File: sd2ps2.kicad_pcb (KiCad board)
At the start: 2 copper layers, 36 x 52.5 mm, 11 parts, among them J1 Conn_01x08, J2 DM3AT-SF-PEJM5, Q1 DTC114T, Q2 DTC114T

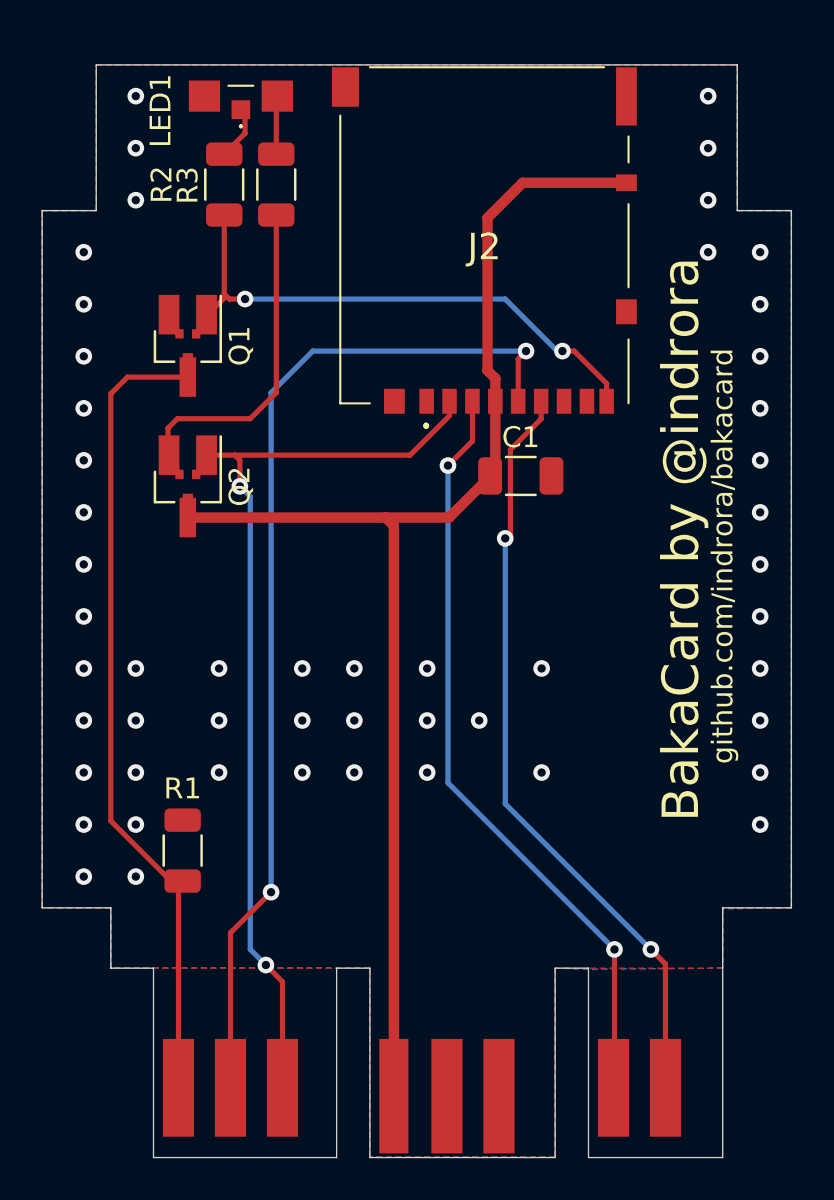
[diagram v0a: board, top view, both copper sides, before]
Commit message: Fix VSS-D0 pin snafu
I misread the instructions on the tin. Ground is important.

also clean up some things that git doesn't need to know about in kicad's world
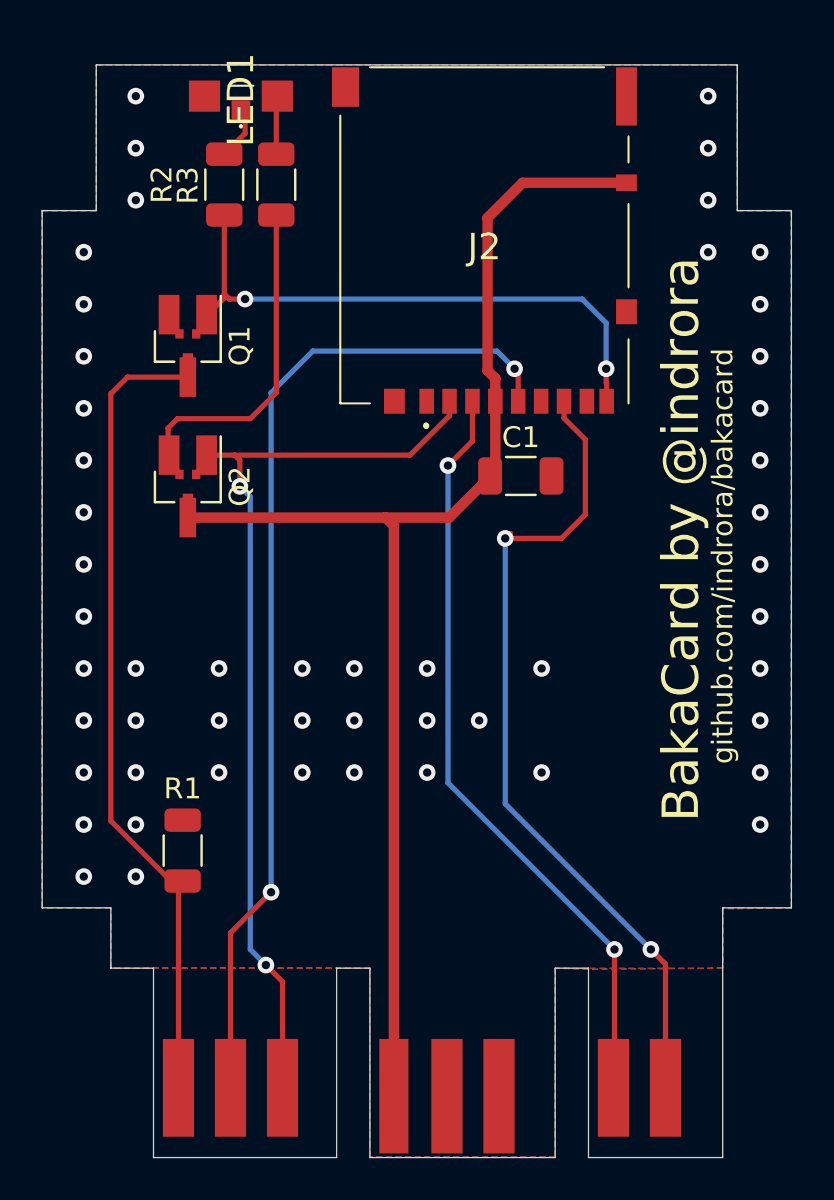
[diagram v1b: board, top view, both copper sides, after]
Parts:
- J1: value Conn_01x08 -> (none)
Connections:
- J1 pad 3: (no net) -> unconnected-(J1-Pad3)
- J2 pad 1: (no net) -> unconnected-(J2-Pad1)
- J2 pad 6: /DO -> GND
- J2 pad 7: (no net) -> /DO
- J2 pad 8: (no net) -> unconnected-(J2-Pad8)
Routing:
- net /DO: track 36.9 -> 40.1 mm
- net /CD: track 26.1 -> 27.8 mm
- net /CLK: track 49.9 -> 48.7 mm

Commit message: rev b
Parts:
- removed R2, R3: 1K, Resistor_SMD:R_1206_3216Metric
- added LED2: LTST-S270KRKT, sd2ps2:LTSTS270KxKT, F.Cu at (171.2, 77.0)
- added RN1: CAY16-1002F4LF, Resistor_SMD:R_Array_Convex_4x1206, F.Cu at (186.9, 100.2)
- added RN2: CAY16-1002F4LF, Resistor_SMD:R_Array_Convex_4x1206, F.Cu at (174.8, 82.5)
- LED1: value LTST-S327KGKFKT -> LTST-S270KGKT; footprint SamacSys_Parts:LTSTS327KGKFKT -> sd2ps2:LTSTS270KxKT
- moved LED1 1.30 mm to (176.2, 77.0), turned to 0 degrees
- moved C1 0.71 mm to (188.0, 96.2)
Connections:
- J2 pad 1: unconnected-(J2-Pad1) -> Net-(J2-Pad1)
- J2 pad 8: unconnected-(J2-Pad8) -> Net-(J2-Pad8)
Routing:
- net +3V3: track 63.4 -> 88.2 mm
- net /CS: track 44.5 -> 53.6 mm
- net Net-(J2-Pad8): track 0.00 -> 8.50 mm
- net Net-(J2-Pad1): track 0.00 -> 7.38 mm
- net Net-(LED2-Pad2): track 0.00 -> 5.58 mm
- net Net-(LED1-Pad2): track 0.00 -> 5.51 mm
- net Net-(LED1-PadA2): track 2.89 -> 0.00 mm
- net Net-(LED1-PadA1): track 2.55 -> 0.00 mm
- net /DO: track 40.1 -> 42.7 mm
- net Net-(Q2-Pad2): track 15.7 -> 15.0 mm
- net GND: vias 52 -> 59
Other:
- board text added: "rev b"
- board text removed: "rev a"

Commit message: rev c
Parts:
- added FID1: Fiducial, Fiducial:Fiducial_0.75mm_Mask1.5mm, F.Cu at (200.0, 117.0)
- added FID2: Fiducial, Fiducial:Fiducial_0.75mm_Mask1.5mm, F.Cu at (168.5, 91.5)
- added FID3: Fiducial, Fiducial:Fiducial_1mm_Mask2mm, F.Cu at (168.5, 117.0)
- REF**: value OSHW-Logo2_7.3x6mm_SilkScreen -> OSHW-Logo2_14.6x12mm_SilkScreen; footprint Symbol:OSHW-Logo2_7.3x6mm_SilkScreen -> Symbol:OSHW-Logo2_14.6x12mm_SilkScreen; moved to F.Cu
- moved R1 21.6 mm to (172.8, 92.2), turned to 0 degrees
- moved REF** 20.2 mm to (175.0, 107.5), turned to 180 degrees
- moved C1 8.68 mm to (179.9, 99.4), turned to -90 degrees
- moved Q2 7.41 mm to (178.7, 92.2)
- moved RN2 5.00 mm to (178.5, 85.9)
- moved J2 4.87 mm to (190.9, 87.3)
- moved RN1 3.73 mm to (184.4, 103.0), turned to 0 degrees
- moved LED2 3.64 mm to (173.8, 79.6)
- moved G*** 3.45 mm to (184.2, 103.0)
- moved LED1 3.39 mm to (178.4, 79.6)
- moved Q1 3.21 mm to (172.8, 86.3)
- moved J1 0.75 mm to (184.2, 128.5)
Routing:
- net +3V3: track 88.2 -> 62.8 mm, vias 0 -> 2
- net Net-(Q2-Pad2): track 15.0 -> 4.75 mm
- net Net-(J2-Pad8): track 8.50 -> 18.3 mm
- net /CS: track 53.6 -> 59.6 mm, vias 2 -> 4
- net /DI: track 36.8 -> 31.8 mm
- net /CD: track 27.4 -> 32.0 mm
- net GND: track 0.00 -> 4.25 mm, vias 59 -> 43
- net /CLK: track 48.7 -> 45.2 mm
- net /DO: track 42.7 -> 40.8 mm
- net Net-(LED2-Pad2): track 5.58 -> 6.84 mm
- net Net-(LED1-Pad2): track 5.51 -> 6.25 mm
- net /ACK: track 39.2 -> 38.6 mm
- net Net-(J2-Pad1): track 7.38 -> 7.91 mm
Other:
- board size 36 x 52.5 mm -> 34.5 x 50 mm
- board text added: "dedicated to Near"
- board text added: "rev c"
- board text removed: "rev b"

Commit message: update tweaks
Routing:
- net /DO: track 40.8 -> 44.3 mm
- net /CS: track 59.6 -> 57.4 mm
- net Net-(J2-Pad1): track 7.91 -> 9.42 mm
- net Net-(J2-Pad8): track 18.3 -> 17.0 mm
- net GND: vias 43 -> 46
